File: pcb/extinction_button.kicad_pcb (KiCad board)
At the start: 2 copper layers, 47.8 x 61.3 mm, 41 parts, among them J1 DX07S016JA1R1500, J2 Conn_01x02, J3 Conn_01x06, SW1 R-667843, U1 ATmega32U4-A, U2 MIC5219-5.0YM5, Y1 ECS-160-10-36-CKM-TR3

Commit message: gerver revision 002
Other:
- board text added: "JLCJLCJLCJLC"
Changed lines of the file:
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@@
       (outputformat 1)
       (mirror false)
-      (drillshape 1)
+      (drillshape 0)
       (scaleselection 1)
-      (outputdirectory "")
+      (outputdirectory "/Users/jayenagrawal/Documents/KiCad/extinction_button/pcb/gerber/")
     )
   )
@@
     (property "Sheetname" "")
     (attr smd)
-    (fp_text reference "F1" (at 1.7 -2) (layer "F.SilkS")
-        (effects (font (size 0.8 0.8) (thickness 0.15)))
+    (fp_text reference "F1" (at 1.84294 -1.883704) (layer "F.SilkS")
+        (effects (font (size 0.5 0.5) (thickness 0.1) bold))
     )
     (fp_text value "MF-USMF050-2" (at 7.144 2.508) (layer "F.Fab")
@@
     (property "ki_keywords" "cap capacitor")
     (attr smd)
-    (fp_text reference "C5" (at -1.484924 -1.06066 45) (layer "F.SilkS")
-        (effects (font (size 1 1) (thickness 0.15)))
+    (fp_text reference "C5" (at -0.688267 -0.806642 45) (layer "F.SilkS")
+        (effects (font (size 0.5 0.5) (thickness 0.1) bold))
     )
     (fp_text value "1uf" (at 0 1.16 45) (layer "F.Fab")
@@
     (property "ki_keywords" "cap capacitor")
     (attr smd)
-    (fp_text reference "C8" (at -2.3 0.1) (layer "F.SilkS")
-        (effects (font (size 1 1) (thickness 0.15)))
+    (fp_text reference "C8" (at -1.75706 0.016296) (layer "F.SilkS")
+        (effects (font (size 0.5 0.5) (thickness 0.1) bold))
     )
     (fp_text value "1uf" (at 0 1.16) (layer "F.Fab")
@@
     (property "ki_keywords" "cap capacitor")
     (attr smd)
-    (fp_text reference "C9" (at -2.3 0.2) (layer "F.SilkS")
-        (effects (font (size 1 1) (thickness 0.15)))
+    (fp_text reference "C9" (at -1.75706 0.016296) (layer "F.SilkS")
+        (effects (font (size 0.5 0.5) (thickness 0.1) bold))
     )
     (fp_text value "100nf" (at 2.625 1.56) (layer "F.Fab")
@@
     (property "ki_keywords" "R res resistor")
     (attr smd)
-    (fp_text reference "R3" (at 0 -1.17 135) (layer "F.SilkS")
-        (effects (font (size 1 1) (thickness 0.15)))
+    (fp_text reference "R3" (at 0.665221 -0.971109 135) (layer "F.SilkS")
+        (effects (font (size 0.5 0.5) (thickness 0.1) bold))
     )
     (fp_text value "10k" (at 0 1.17 135) (layer "F.Fab")
@@
         (effects (font (size 1.27 1.27) (thickness 0.15)))
     )
-    (pad "1" thru_hole rect (at 0 0) (size 0.65 0.65) (drill 0.6) (layers "*.Cu" "*.Mask"))
+    (pad "1" thru_hole rect (at 0 0) (size 0.8 0.8) (drill 0.6) (layers "*.Cu" "*.Mask"))
   )
   (footprint "LED_SMD:LED_WS2812B_PLCC4_5.0x5.0mm_P3.2mm" (layer "F.Cu")
@@
     (property "ki_keywords" "cap capacitor")
     (attr smd)
-    (fp_text reference "C7" (at 2.7 -2.2) (layer "F.SilkS")
-        (effects (font (size 1 1) (thickness 0.15)))
+    (fp_text reference "C7" (at 3.24294 -1.283704) (layer "F.SilkS")
+        (effects (font (size 0.5 0.5) (thickness 0.1) bold))
     )
     (fp_text value "10uf" (at 0 2.35) (layer "F.Fab")
@@
     (fp_line (start 1.75 1.4) (end 1.75 -1.4)
       (stroke (width 0.1) (type solid)) (layer "F.Fab"))
-    (pad "1" smd roundrect (at -1.625 0) (size 1.5 2.35) (layers "F.Cu" "F.Paste" "F.Mask") (roundrect_rratio 0.166667)
+    (pad "1" smd roundrect (at -1.625 0) (size 1.5 2.35) (layers "F.Cu" "F.Paste" "F.Mask") (roundrect_rratio 0.1666673333)
       (net 8 "VCC") (pintype "passive"))
-    (pad "2" smd roundrect (at 1.625 0) (size 1.5 2.35) (layers "F.Cu" "F.Paste" "F.Mask") (roundrect_rratio 0.166667)
+    (pad "2" smd roundrect (at 1.625 0) (size 1.5 2.35) (layers "F.Cu" "F.Paste" "F.Mask") (roundrect_rratio 0.1666673333)
       (net 1 "GND") (pintype "passive"))
     (model "${KICAD6_3DMODEL_DIR}/Capacitor_Tantalum_SMD.3dshapes/CP_EIA-3528-15_AVX-H.wrl"
@@
     (property "Sheetname" "")
     (attr smd)
-    (fp_text reference "J1" (at -2.9 1.2 90) (layer "F.SilkS")
+    (fp_text reference "J1" (at -2.983704 1.2 90) (layer "F.SilkS")
         (effects (font (size 1 1) (thickness 0.15)))
     )
@@
     (property "ki_keywords" "R res resistor")
     (attr smd)
-    (fp_text reference "R5" (at 2.05061 0.070711 135) (layer "F.SilkS")
-        (effects (font (size 1 1) (thickness 0.15)))
+    (fp_text reference "R5" (at 1.668232 0.051871 135) (layer "F.SilkS")
+        (effects (font (size 0.5 0.5) (thickness 0.1) bold))
     )
     (fp_text value "330" (at 0 1.17 135) (layer "F.Fab")
@@
     (property "ki_keywords" "cap capacitor")
     (attr smd)
-    (fp_text reference "C4" (at 0.268528 -1.428528 135) (layer "F.SilkS")
-        (effects (font (size 1 1) (thickness 0.15)))
+    (fp_text reference "C4" (at 0.665221 -0.971109 315) (layer "F.SilkS")
+        (effects (font (size 0.5 0.5) (thickness 0.1) bold))
     )
     (fp_text value "100nf" (at 0 1.16 135) (layer "F.Fab")
@@
     (property "ki_keywords" "500mA ultra-low-noise LDO linear voltage regulator fixed positive")
     (attr smd)
-    (fp_text reference "U2" (at -1.5 2.3 90) (layer "F.SilkS")
-        (effects (font (size 1 1) (thickness 0.15)))
+    (fp_text reference "U2" (at 1.616296 2.05706 90) (layer "F.SilkS")
+        (effects (font (size 0.5 0.5) (thickness 0.1) bold))
     )
     (fp_text value "MIC5219-5.0YM5" (at 0 2.4 90) (layer "F.Fab")
@@
     (property "ki_keywords" "LTST-C191KSKT")
     (attr smd)
-    (fp_text reference "LED1" (at -0.209015 -1.697056 45 unlocked) (layer "F.SilkS")
-        (effects (font (size 1 1) (thickness 0.15)))
+    (fp_text reference "LED1" (at 0.620673 -1.173257 45 unlocked) (layer "F.SilkS")
+        (effects (font (size 0.5 0.5) (thickness 0.1) bold))
     )
     (fp_text value "LTST-C191KSKT" (at 0 0 -135 unlocked) (layer "F.Fab")
@@
     (property "ki_keywords" "R res resistor")
     (attr smd)
-    (fp_text reference "R4" (at -0.353553 -1.767767 45) (layer "F.SilkS")
-        (effects (font (size 1 1) (thickness 0.15)))
+    (fp_text reference "R4" (at 0.688267 -1.031836 45) (layer "F.SilkS")
+        (effects (font (size 0.5 0.5) (thickness 0.1) bold))
     )
     (fp_text value "330" (at 0 1.17 45) (layer "F.Fab")
@@
     (property "ki_keywords" "cap capacitor")
     (attr smd)
-    (fp_text reference "C3" (at 2.1 0.1) (layer "F.SilkS")
-        (effects (font (size 1 1) (thickness 0.15)))
+    (fp_text reference "C3" (at 1.74294 0.016296) (layer "F.SilkS")
+        (effects (font (size 0.5 0.5) (thickness 0.1) bold))
     )
     (fp_text value "22pf" (at 0 1.16) (layer "F.Fab")
@@
     (property "ki_keywords" "LTST-C191KSKT")
     (attr smd)
-    (fp_text reference "LED3" (at 0 -1.5 unlocked) (layer "F.SilkS")
-        (effects (font (size 1 1) (thickness 0.15)))
+    (fp_text reference "LED3" (at 0.55706 1.083704 unlocked) (layer "F.SilkS")
+        (effects (font (size 0.5 0.5) (thickness 0.1) bold))
     )
     (fp_text value "LTST-C191KSKT" (at 0 0 180 unlocked) (layer "F.Fab")
@@
     (property "ki_keywords" "cap capacitor")
     (attr smd)
-    (fp_text reference "C6" (at -3.3 0.7) (layer "F.SilkS")
-        (effects (font (size 1 1) (thickness 0.15)))
+    (fp_text reference "C6" (at 0.016296 -2.24294) (layer "F.SilkS")
+        (effects (font (size 0.5 0.5) (thickness 0.1) bold))
     )
     (fp_text value "10uf" (at 0 2.35 90) (layer "F.Fab")
@@
     (fp_line (start 1.75 1.4) (end 1.75 -1.4)
       (stroke (width 0.1) (type solid)) (layer "F.Fab"))
-    (pad "1" smd roundrect (at -1.625 0 270) (size 1.5 2.35) (layers "F.Cu" "F.Paste" "F.Mask") (roundrect_rratio 0.166667)
+    (pad "1" smd roundrect (at -1.625 0 270) (size 1.5 2.35) (layers "F.Cu" "F.Paste" "F.Mask") (roundrect_rratio 0.1666673333)
       (net 7 "Net-(U2-EN)") (pintype "passive"))
-    (pad "2" smd roundrect (at 1.625 0 270) (size 1.5 2.35) (layers "F.Cu" "F.Paste" "F.Mask") (roundrect_rratio 0.166667)
+    (pad "2" smd roundrect (at 1.625 0 270) (size 1.5 2.35) (layers "F.Cu" "F.Paste" "F.Mask") (roundrect_rratio 0.1666673333)
       (net 1 "GND") (pintype "passive"))
     (model "${KICAD6_3DMODEL_DIR}/Capacitor_Tantalum_SMD.3dshapes/CP_EIA-3528-15_AVX-H.wrl"
@@
     (property "ki_keywords" "LTST-C191KSKT")
     (attr smd)
-    (fp_text reference "LED2" (at -0.070711 1.343503 315 unlocked) (layer "F.SilkS")
-        (effects (font (size 1 1) (thickness 0.15)))
+    (fp_text reference "LED2" (at -0.536861 1.0795 315 unlocked) (layer "F.SilkS")
+        (effects (font (size 0.5 0.5) (thickness 0.1) bold))
     )
     (fp_text value "LTST-C191KSKT" (at 0 0 135 unlocked) (layer "F.Fab")
@@
     (property "ki_keywords" "AVR 8bit Microcontroller MegaAVR USB")
     (attr smd)
-    (fp_text reference "U1" (at 0 -7.45 45) (layer "F.SilkS")
-        (effects (font (size 1 1) (thickness 0.15)))
+    (fp_text reference "U1" (at 0.01884 -7.170603 45) (layer "F.SilkS")
+        (effects (font (size 0.5 0.5) (thickness 0.1) bold))
     )
     (fp_text value "ATmega32U4-A" (at 0 7.45 45) (layer "F.Fab")
@@
     (property "ki_keywords" "R res resistor")
     (attr smd)
-    (fp_text reference "R2" (at -0.0025 1.3) (layer "F.SilkS")
-        (effects (font (size 1 1) (thickness 0.15)))
+    (fp_text reference "R2" (at 1.63794 0.316296) (layer "F.SilkS")
+        (effects (font (size 0.5 0.5) (thickness 0.1) bold))
     )
     (fp_text value "22" (at 0 1.17) (layer "F.Fab")
@@
     (property "ki_keywords" "cap capacitor")
     (attr smd)
-    (fp_text reference "C1" (at 2.2 -0.1) (layer "F.SilkS")
-        (effects (font (size 1 1) (thickness 0.15)))
+    (fp_text reference "C1" (at 1.85706 -0.016296) (layer "F.SilkS")
+        (effects (font (size 0.5 0.5) (thickness 0.1) bold))
     )
     (fp_text value "22pf" (at 0 1.16) (layer "F.Fab")
@@
     )
   )
+  (gr_text "JLCJLCJLCJLC" (at 178.9 102.5 90) (layer "B.SilkS")
+    (effects (font (size 0.8 0.8) (thickness 0.15) bold) (justify left bottom))
+  )
   (gr_text "vcc    gnd    sck    miso    mosi    rst" (at 178.25706 48.483704) (layer "F.SilkS")

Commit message: gerber rev 003
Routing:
- net VBUS: track 52.7 -> 54.1 mm
- net Net-(U2-EN): track 13.0 -> 13.6 mm
- net GND: track 66.4 -> 66.6 mm, vias 15 -> 16

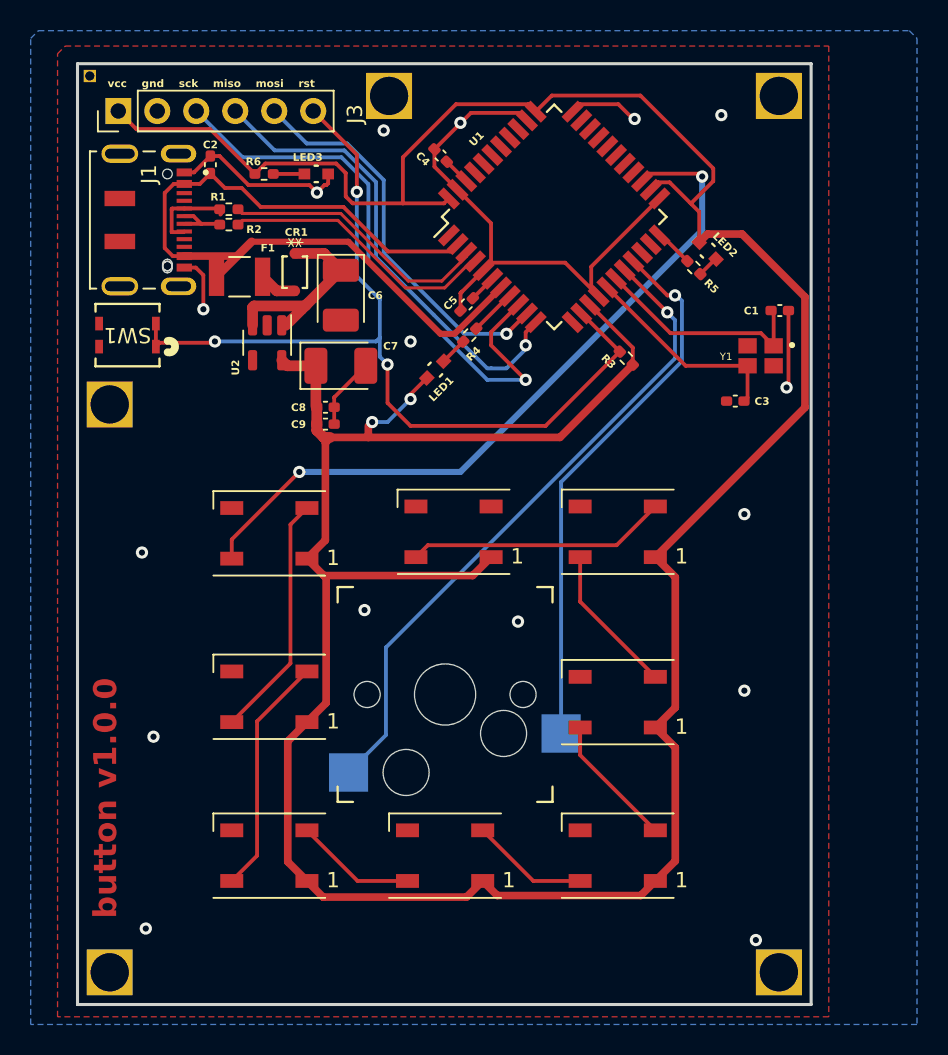
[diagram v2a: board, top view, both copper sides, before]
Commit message: add reverse mounted led
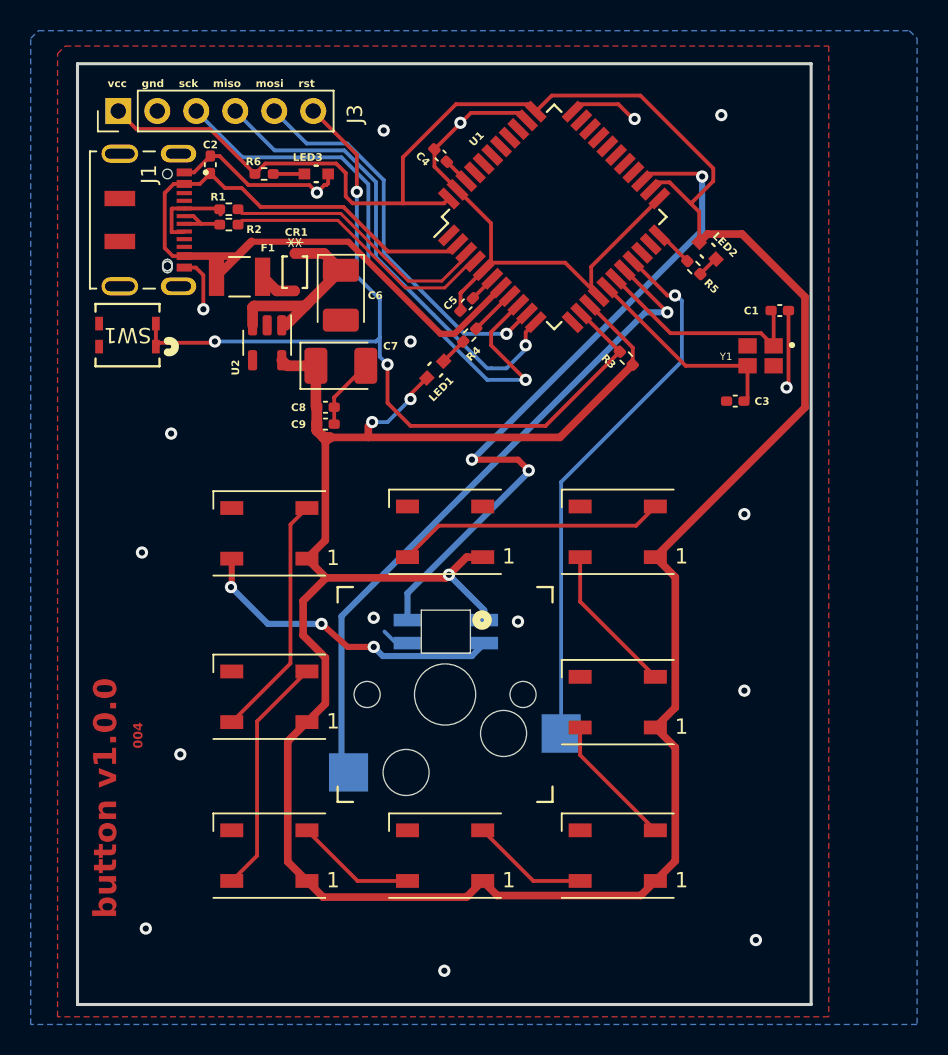
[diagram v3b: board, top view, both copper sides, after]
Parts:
- removed ? (x6): , 
- added LED4: 4960, SK6812-E:4960_ADA, B.Cu at (200.3, 83.9)
- moved D8 0.55 mm to (200.2, 77.4)
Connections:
- D7 pad 4: D4 -> Net-(D7-DIN)
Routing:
- net Net-(D7-DIN): track 0.00 -> 20.9 mm, vias 0 -> 3
- net VCC: track 224.3 -> 229.0 mm, vias 2 -> 3
- net GND: track 66.6 -> 68.4 mm, vias 16 -> 18
- net D4: track 47.9 -> 46.1 mm, vias 2 -> 3
- net D3: track 42.9 -> 43.7 mm
- net Net-(D1-DOUT): track 17.0 -> 17.5 mm
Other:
- board text added: "004"
